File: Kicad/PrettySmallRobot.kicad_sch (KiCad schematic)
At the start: 22 parts

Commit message: added antenna match circuit
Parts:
- added C?: C, symbol Device:C
- added C?: (no value), symbol Device:C
- added L?: (no value), symbol Device:L
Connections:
- net +BATT: now also J?.1 (Pin_1)
- net GND: now also J?.2 (Pin_2), U?.4 (GND), U?.4 (GND), U?.9 (GND), U?.9 (GND), C?.2, C?.2
- net at U?.2 (LNA_IN/RF): now also C?.1, L?.2
- net at AE?.1 (A): now also C?.1, L?.1
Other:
- moved on the sheet: AE?, J?, U?

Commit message: schematic progressed
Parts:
- removed U?: DRV8837, Package_SON:WSON-8-1EP_2x2mm_P0.5mm_EP0.9x1.6mm, symbol Driver_Motor:DRV8837
- added C? (x4): C, symbol Device:C
- added U?: DRV8837, Package_SON:WSON-8-1EP_2x2mm_P0.5mm_EP0.9x1.6mm, symbol Driver_Motor:DRV8837
- J?: value USB_C_Receptacle_USB2.0 -> (none); LCSC C283540 -> C134092
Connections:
- net +3V3: now also U?.7 (~{SLEEP}), U?.8 (VCC), C?.1, C?.1, C?.1, C?.1, U?.7 (~{SLEEP}), U?.8 (VCC)
- net +BATT: now also U?.1 (VM), U?.1 (VM)
- net GND: now also C?.2, C?.2, C?.2, C?.2, U?.4 (GND), U?.9 (GND)
- net MOTORA_OUT1: now reaches J?.1 (Pin_1)
- net MOTORA_OUT1: now also U?.2 (OUT1)
- net MOTORA_OUT2: now reaches J?.2 (Pin_2)
- net MOTORA_OUT2: now also U?.3 (OUT2)
- net MOTORA_IN1: now reaches U?.5 (IN2)
- net MOTORA_IN1: now also U?.6 (IN1)
- net MOTORB_OUT1: now reaches J?.1 (Pin_1)
- net MOTORB_OUT1: now also U?.2 (OUT1)
- net MOTORB_OUT2: now reaches J?.2 (Pin_2)
- net MOTORB_OUT2: now also U?.3 (OUT2)
- new net MOTORB_IN1: U?.5 (IN2), U?.6 (IN1)
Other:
- note added: "3.7V Lipo (3-4.2V)"
- note added: "Motor A"
- note added: "Motor B"
- note removed: "Battery"
- note removed: "Motor 1"
- note removed: "Motor 2"

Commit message: progressed schematic
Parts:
- removed J?: (no value), symbol Connector:USB_C_Receptacle_USB2.0
- added J?: (no value), symbol Kicad_symbols:TYPE-C-31-M-12
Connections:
- new net: J?.A1_B12 (GND), J?.B1_A12 (GND)
- new net: J?.A4_B9 (VBUS), J?.B4_A9 (VBUS)
- new net: J?.S1 (SHIELD), J?.S2 (SHIELD), J?.S3 (SHIELD), J?.S4 (SHIELD)
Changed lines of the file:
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@@
     (pin "1")
+  )
+  (symbol (lib_id "Kicad_symbols:TYPE-C-31-M-12") (at 34.29 41.91 0) (unit 1)
+    (in_bom yes) (on_board yes) (fields_autoplaced)
+    (property "Reference" "J?" (id 0) (at 34.29 24.13 0))
+    (property "Value" "" (id 1) (at 34.29 26.67 0))
+    (property "Footprint" "" (id 2) (at -5.08 35.56 0)
+      (effects (font (size 1.27 1.27)) (justify bottom) hide)
+    )
+    (property "Datasheet" "" (id 3) (at 34.29 41.91 0)
+      (effects (font (size 1.27 1.27)) hide)
+    )
+    (property "PARTREV" "2020.12.08" (id 4) (at 34.29 36.83 0)
+      (effects (font (size 1.27 1.27)) (justify bottom) hide)
+    )
+    (property "SNAPEDA_PN" "TYPE-C-31-M-12" (id 5) (at 34.29 29.21 0)
+      (effects (font (size 1.27 1.27)) (justify bottom) hide)
+    )
+    (property "MANUFACTURER" "" (id 6) (at 34.29 59.69 0)
+      (effects (font (size 1.27 1.27)) (justify bottom) hide)
+    )
+    (property "STANDARD" "" (id 7) (at -3.81 52.07 0)
+      (effects (font (size 1.27 1.27)) (justify bottom) hide)
+    )
+    (property "MAXIMUM_PACKAGE_HEIGHT" "" (id 8) (at -8.89 41.91 0)
+      (effects (font (size 1.27 1.27)) (justify bottom) hide)
+    )
+    (property "LCSC" "C165948" (id 9) (at 34.29 41.91 0)
+      (effects (font (size 1.27 1.27)) hide)
+    )
+    (pin "A1_B12")
+    (pin "A4_B9")
+    (pin "A5")
+    (pin "A6")
+    (pin "A7")
+    (pin "A8")
+    (pin "B1_A12")
+    (pin "B4_A9")
+    (pin "B5")
+    (pin "B6")
+    (pin "B7")
+    (pin "B8")
+    (pin "S1")
+    (pin "S2")
+    (pin "S3")
+    (pin "S4")
   )
   (symbol (lib_id "Device:D_Schottky") (at 154.305 24.765 180) (unit 1)
@@
     (pin "2")
   )
-  (symbol (lib_id "Connector:USB_C_Receptacle_USB2.0") (at 35.56 44.45 0) (unit 1)
-    (in_bom yes) (on_board yes) (fields_autoplaced)
-    (property "Reference" "J?" (id 0) (at 35.56 21.59 0))
-    (property "Value" "" (id 1) (at 35.56 24.13 0))
-    (property "Footprint" "" (id 2) (at 39.37 44.45 0)
-      (effects (font (size 1.27 1.27)) hide)
-    )
-    (property "Datasheet" "https://www.usb.org/sites/default/files/documents/usb_type-c.zip" (id 3) (at 39.37 44.45 0)
-      (effects (font (size 1.27 1.27)) hide)
-    )
-    (property "LCSC" "C134092" (id 4) (at 35.56 44.45 0)
-      (effects (font (size 1.27 1.27)) hide)
-    )
-    (pin "A1")
-    (pin "A12")
-    (pin "A4")
-    (pin "A5")
-    (pin "A6")
-    (pin "A7")
-    (pin "A8")
-    (pin "A9")
-    (pin "B1")
-    (pin "B12")
-    (pin "B4")
-    (pin "B5")
-    (pin "B6")
-    (pin "B7")
-    (pin "B8")
-    (pin "B9")
-    (pin "S1")
-  )
   (symbol (lib_id "power:+BATT") (at 217.17 111.76 0) (unit 1)
     (in_bom yes) (on_board yes)
@@
       (reference "D?") (unit 1) (value "D_Schottky") (footprint "")
     )
+    (path "/3c6b0d4e-fccc-417e-bf34-f237c07621e0"
+      (reference "J?") (unit 1) (value "TYPE-C-31-M-12") (footprint "")
+    )
     (path "/3df40196-e4fa-42be-bb30-c5850f257a4a"
       (reference "J?") (unit 1) (value "S2B-PH-K-S(LF)(SN)") (footprint "")
@@
       (reference "J?") (unit 1) (value "S2B-PH-K-S(LF)(SN)") (footprint "")
     )
-    (path "/9eacbb2d-50b8-4118-adfc-424ecd01793d"
-      (reference "J?") (unit 1) (value "USB_C_Receptacle_USB2.0") (footprint "")
-    )
     (path "/251ade2c-e1c8-4335-ab15-b1573b3e543c"

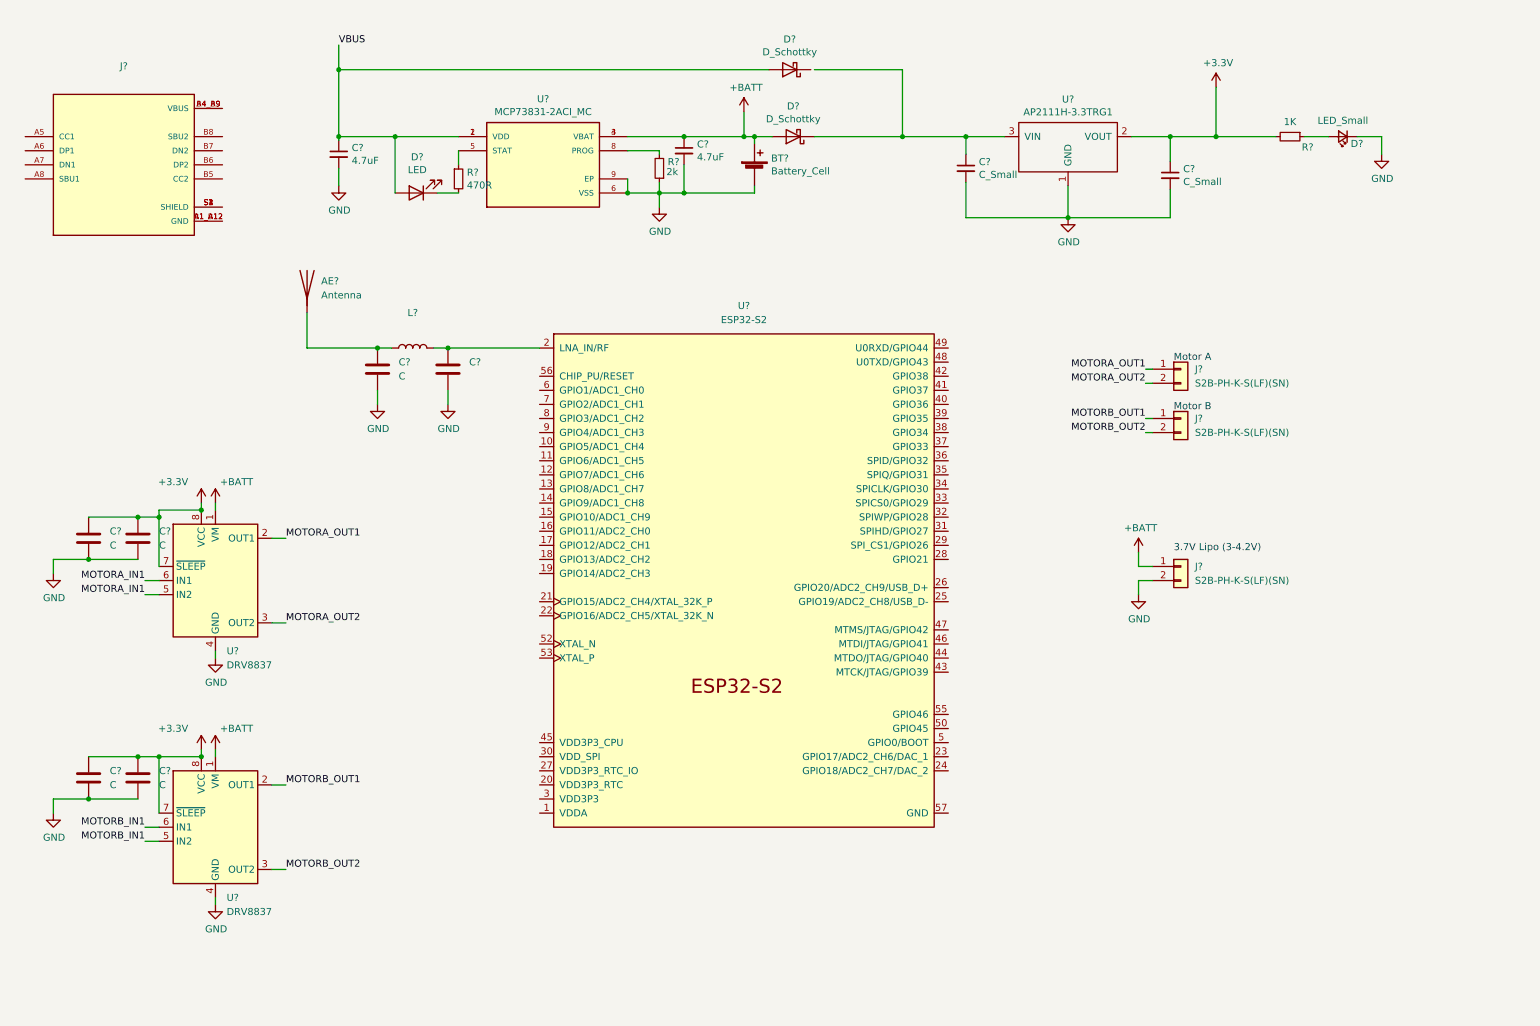
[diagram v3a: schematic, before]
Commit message: usb c nets done, started on esp32 nets
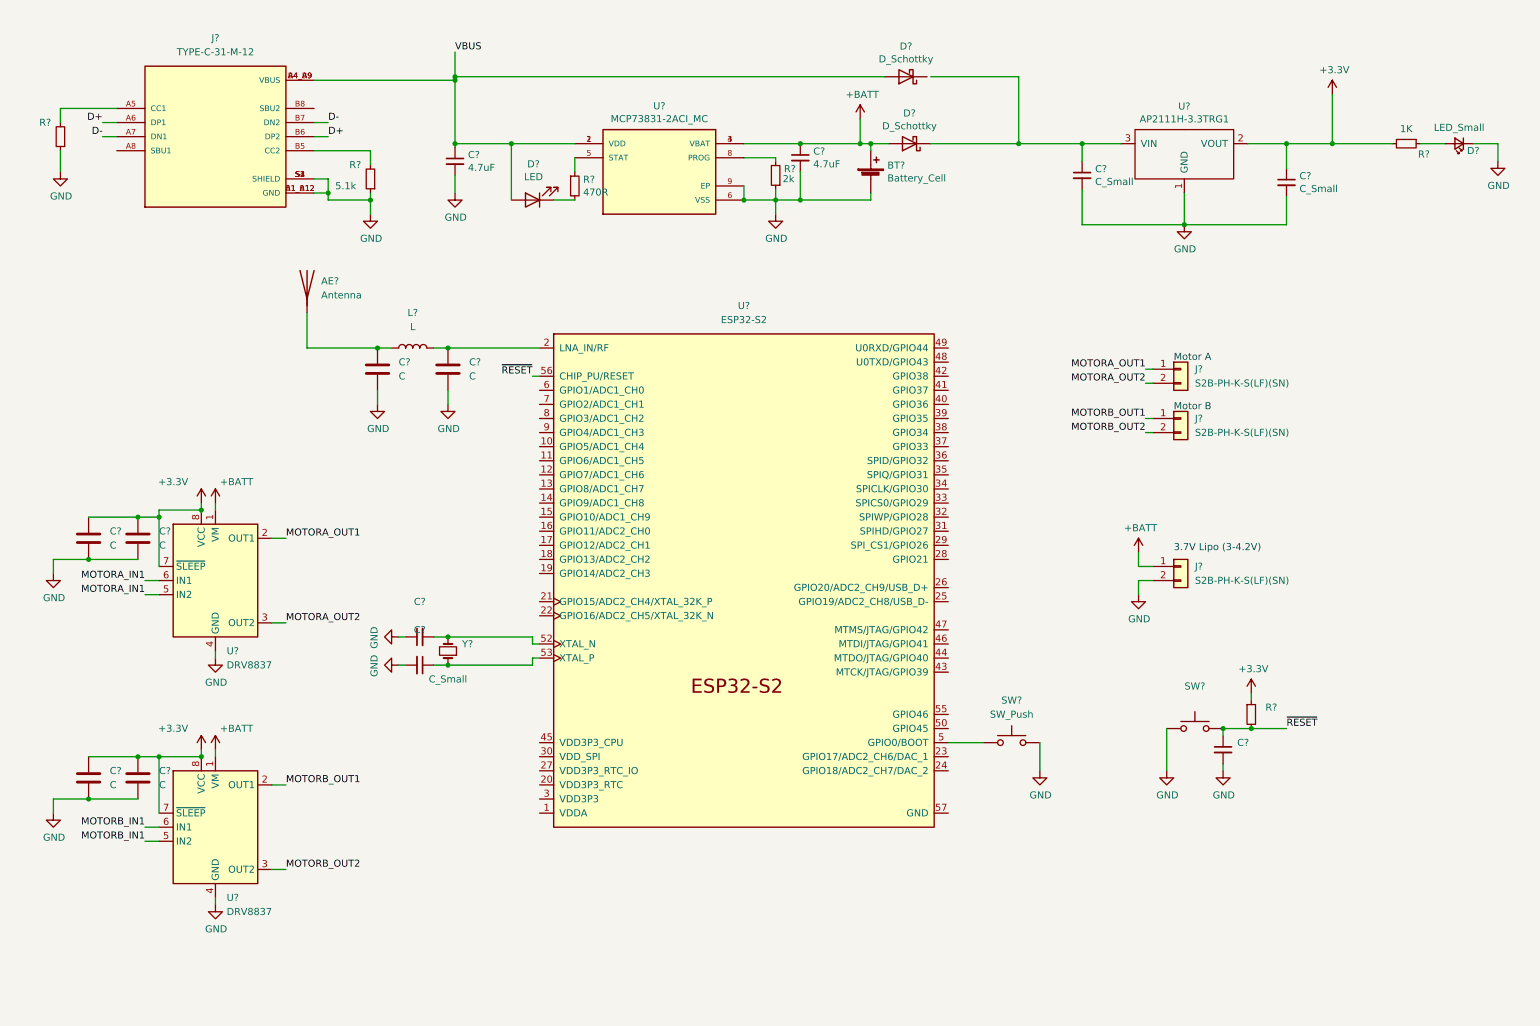
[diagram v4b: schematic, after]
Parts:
- added C?: C_Small, symbol Device:C_Small
- added C? (x2): (no value), symbol Device:C_Small
- added R?: 5.1k, symbol Device:R_Small
- added R? (x2): (no value), symbol Device:R_Small
- added SW?: (no value), symbol Switch:SW_Push
- added SW?: SW_Push, symbol Switch:SW_Push
- added Y?: (no value), symbol Device:Crystal_Small
- C?: value (none) -> C
- J?: value (none) -> TYPE-C-31-M-12
- L?: value (none) -> L
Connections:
- net +3V3: now also R?.1
- net GND: now also J?.A1_B12 (GND), J?.B1_A12 (GND), J?.S1 (SHIELD), J?.S2 (SHIELD), J?.S3 (SHIELD), J?.S4 (SHIELD), C?.1, C?.2, C?.2, R?.1, R?.1, SW?.1, SW?.2
- net VBUS: now also J?.A4_B9 (VBUS), J?.B4_A9 (VBUS)
- net at J?.A5 (CC1): now also R?.2
- net D+: now reaches J?.A6 (DP1)
- net D+: now also J?.B6 (DP2)
- net D-: now reaches J?.A7 (DN1)
- net D-: now also J?.B7 (DN2)
- net at J?.B5 (CC2): now also R?.2
- net at U?.5 (GPIO0/BOOT): now also SW?.1
- net at U?.52 (XTAL_N): now also C?.2, Y?.2
- net at U?.53 (XTAL_P): now also C?.1, Y?.1
- net ~{RESET}: now reaches U?.56 (CHIP_PU/RESET)
- net ~{RESET}: now also C?.1, R?.2, SW?.2
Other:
- moved on the sheet: BT?, C?, D?, J?, R?, U?

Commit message: progressed esp32 schem nets
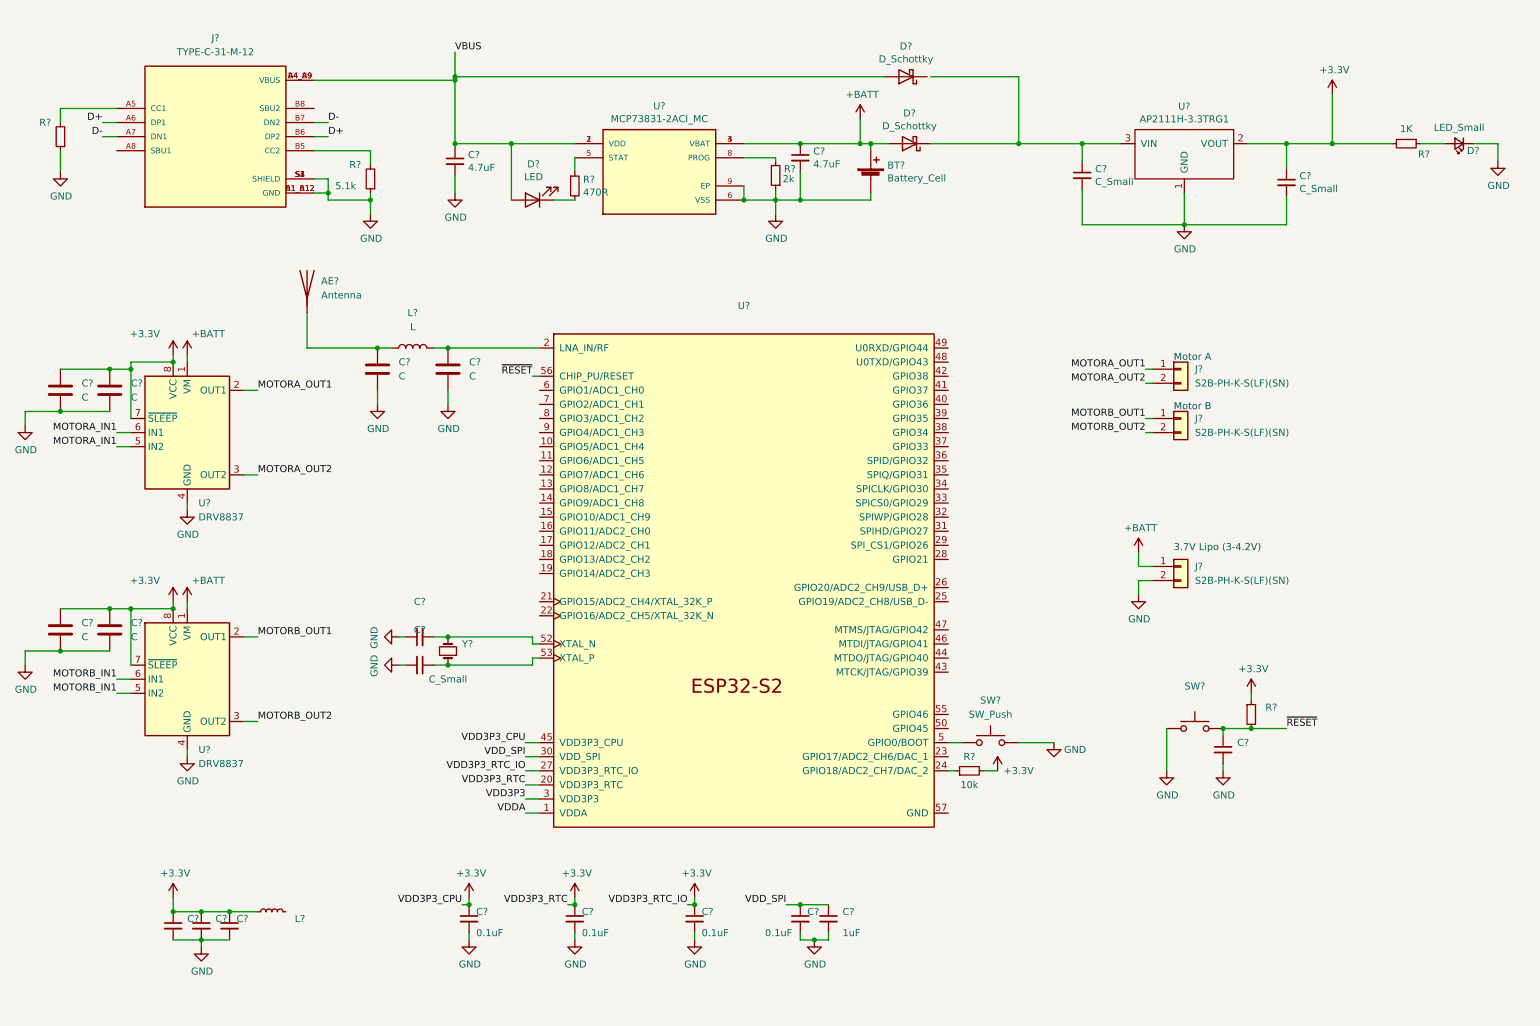
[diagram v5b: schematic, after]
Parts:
- added C? (x3): (no value), symbol Device:C_Small
- added C? (x4): 0.1uF, symbol Device:C_Small
- added C?: 1uF, symbol Device:C_Small
- added L?: (no value), symbol Device:L_Small
- added R?: 10k, symbol Device:R_Small
- U?: value ESP32-S2 -> (none); footprint Package_DFN_QFN:QFN-56-1EP_7x7mm_P0.4mm_EP5.6x5.6mm -> (none)
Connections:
- net +3V3: now also U?.20 (VDD3P3_RTC), U?.27 (VDD3P3_RTC_IO), U?.45 (VDD3P3_CPU), C?.1, C?.1, C?.1, C?.1, C?.1, C?.1, L?.1, R?.2
- net GND: now also C?.2, C?.2, C?.2, C?.2, C?.2, C?.2, C?.2, C?.2
- net VDDA: now reaches U?.1 (VDDA), U?.51 (VDDA), U?.54 (VDDA)
- net at U?.24 (GPIO18/ADC2_CH7/DAC_2): now also R?.1
- net VDD3P3: now reaches U?.3 (VDD3P3), U?.4 (VDD3P3)
- net VDD_SPI: now reaches U?.30 (VDD_SPI)
- net VDD_SPI: now also C?.1, C?.1
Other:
- moved on the sheet: C?, SW?, U?

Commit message: cleaned up schematic - added boxes around sections etc
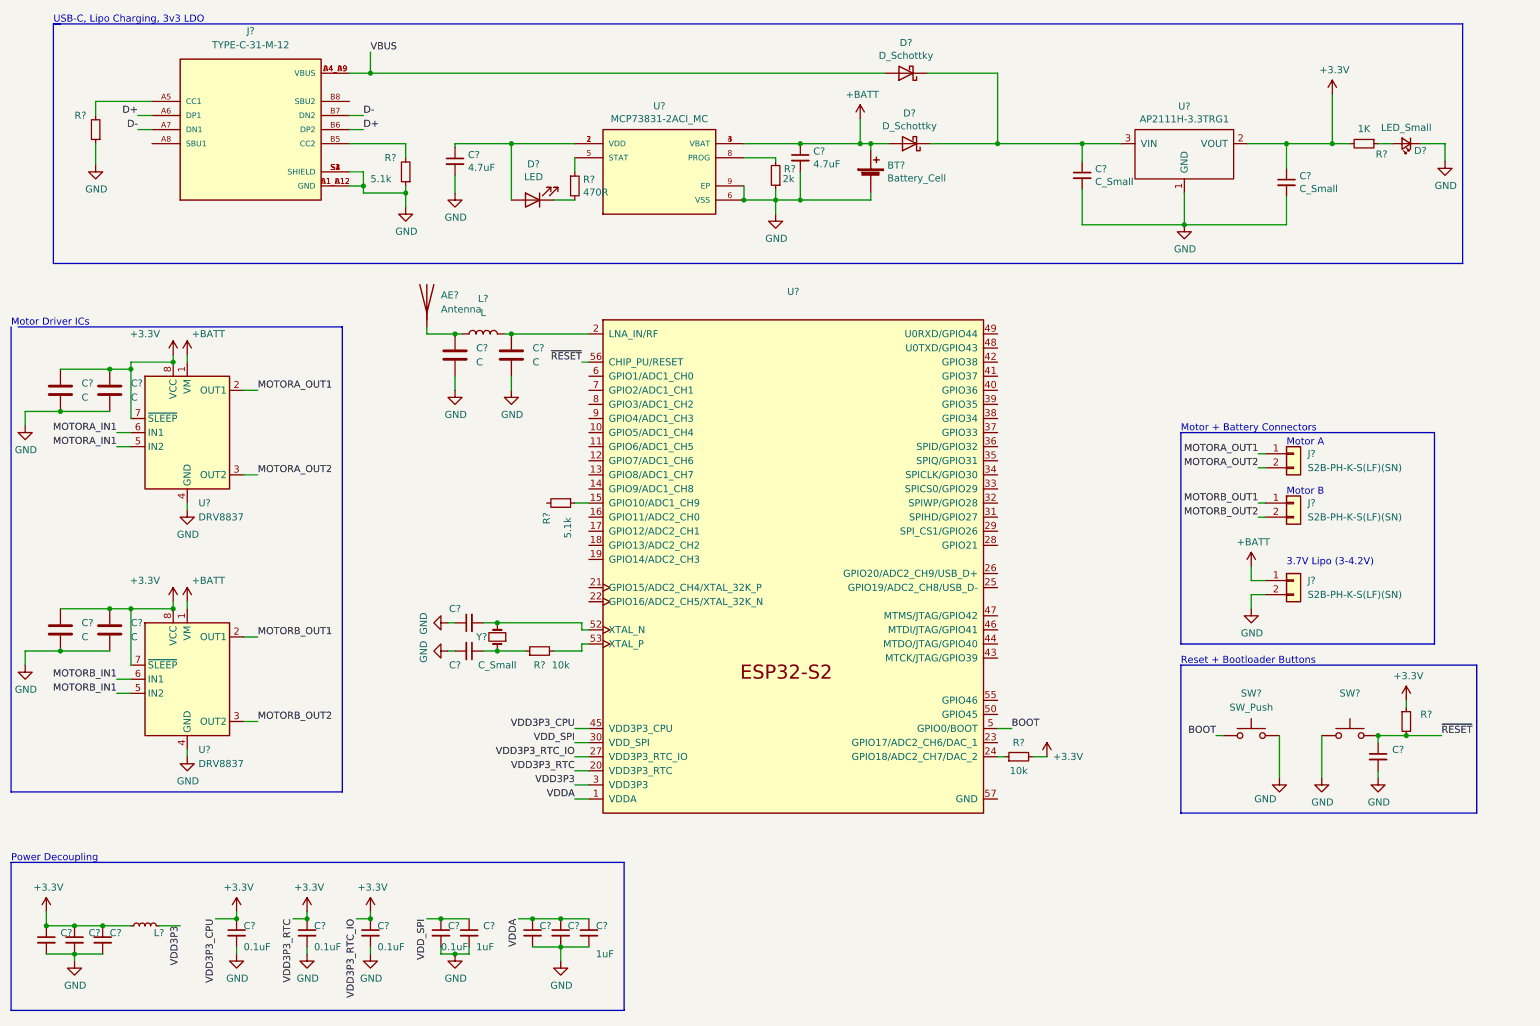
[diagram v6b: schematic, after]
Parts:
- removed SW?: SW_Push, symbol Switch:SW_Push
- added C? (x2): (no value), symbol Device:C_Small
- added C?: 1uF, symbol Device:C_Small
- added R?: 10k, symbol Device:R_Small
- added R?: 5.1k, symbol Device:R_Small
- added SW?: SW_Push, symbol Switch:SW_Push
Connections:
- net GND: now also C?.2, C?.2, C?.2, SW?.2
- net VBUS: no longer C?.1, D?.2 (A), U?.1 (VDD), U?.2 (VDD)
- net VDD3P3: now also L?.2
- net VDDA: now also C?.1, C?.1, C?.1
- net at D?.1 (K): now also C?.1, D?.1 (K), U?.3 (VIN)
- net at C?.1, Y?.1: now also R?.1; no longer U?.53 (XTAL_P)
- net at U?.15 (GPIO10/ADC1_CH9): now also R?.1
- net BOOT: now reaches U?.5 (GPIO0/BOOT)
- net BOOT: now also SW?.1
- new net: C?.1, D?.2 (A), U?.1 (VDD), U?.2 (VDD)
- new net: R?.2, U?.53 (XTAL_P)
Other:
- note added: "Motor + Battery Connectors"
- note added: "Motor Driver ICs"
- note added: "Power Decoupling"
- note added: "Reset + Bootloader Buttons"
- note added: "USB-C, Lipo Charging, 3v3 LDO"
- moved on the sheet: AE?, C?, D?, J?, L?, R?, SW?, U?, Y?
